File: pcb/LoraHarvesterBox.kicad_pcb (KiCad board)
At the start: 4 copper layers, 48 x 45.5 mm, 44 parts, among them J1 Conn_01x02_Pin, J2 Conn_01x02_Pin, J3 Conn_01x02_Pin, J4 Conn_01x04_Socket, J5 Conn_01x04_Socket, J6 Conn_01x04_Socket, J7 Conn_01x04_Socket, J8 Conn_01x06_Socket, SW1 SSSS811101, SW2 TS-1088-AR02016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

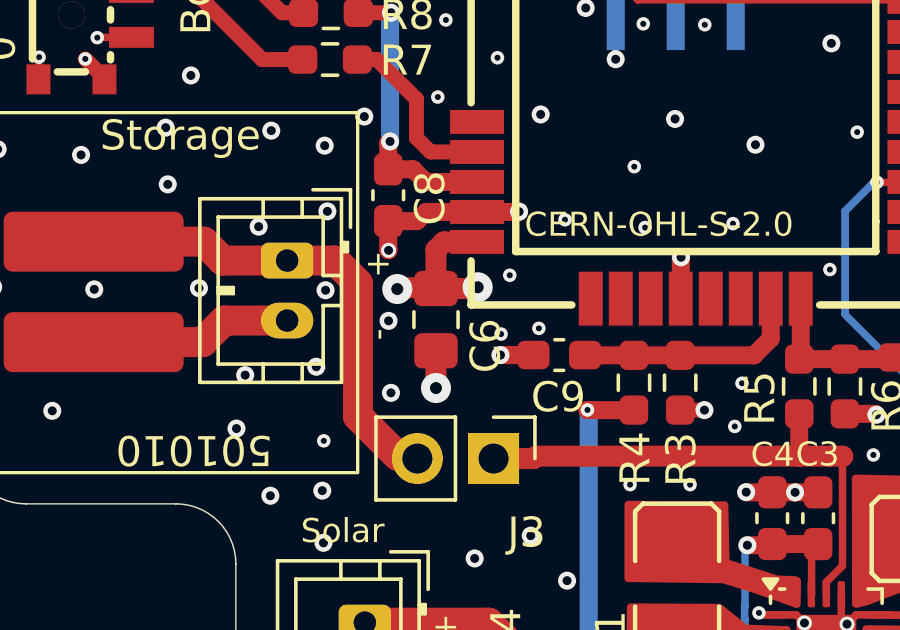
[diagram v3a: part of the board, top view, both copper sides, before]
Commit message: pcb, sch, doc: remove C as RAK31762 has 10uF+100nF already internally
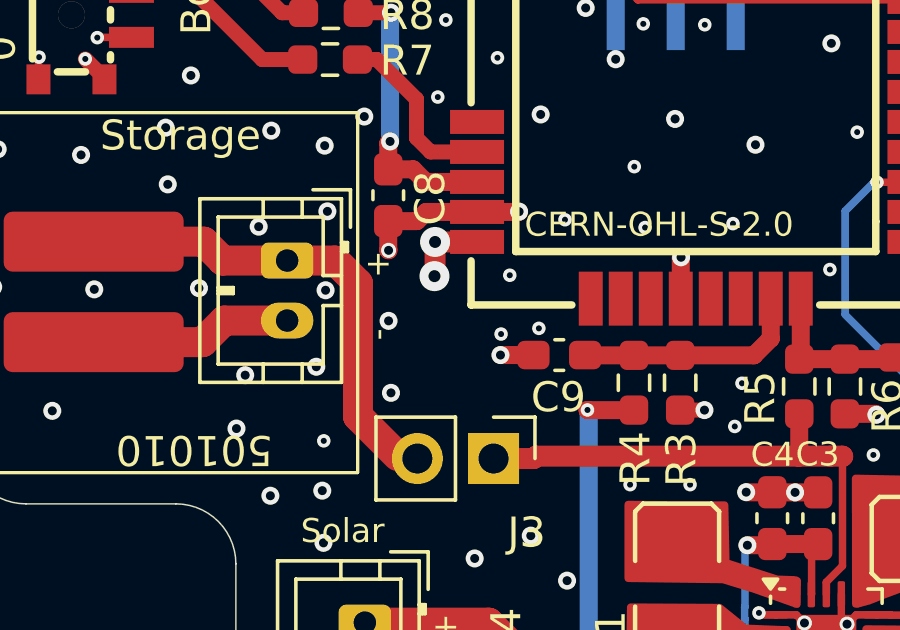
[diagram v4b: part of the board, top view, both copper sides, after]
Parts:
- removed C6: C, Capacitor_SMD:C_0805_2012Metric_Pad1.18x1.45mm_HandSolder
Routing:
- net +3V0: track 16.0 -> 13.1 mm
- net GND: track 59.4 -> 58.1 mm, vias 186 -> 185
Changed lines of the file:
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@@
 		)
 	)
-	(footprint "Capacitor_SMD:C_0805_2012Metric_Pad1.18x1.45mm_HandSolder"
-		(layer "F.Cu")
-		(at 116.67 82.86 90)
-		(descr "Capacitor SMD 0805 (2012 Metric), square (rectangular) end terminal, IPC-7351 nominal with elongated pad for handsoldering. (Body size source: IPC-SM-782 page 76, https://www.pcb-3d.com/wordpress/wp-content/uploads/ipc-sm-782a_amendment_1_and_2.pdf, https://docs.google.com/spreadsheets/d/1BsfQQcO9C6DZCsRaXUlFlo91Tg2WpOkGARC1WS5S8t0/edit?usp=sharing), generated with kicad-footprint-generator")
-		(tags "capacitor handsolder")
-		(property "Reference" "C6"
-			(at -0.87 1.66 90)
-			(layer "F.SilkS")
-			(effects
-				(font
-					(size 1 1)
-					(thickness 0.15)
-				)
-			)
-		)
-		(property "Value" "C"
-			(at 0 1.68 90)
-			(layer "F.Fab")
-			(hide yes)
-			(effects
-				(font
-					(size 1 1)
-					(thickness 0.15)
-				)
-			)
-		)
-		(property "Datasheet" "~"
-			(at 0 0 90)
-			(layer "F.Fab")
-			(hide yes)
-			(effects
-				(font
-					(size 1.27 1.27)
-					(thickness 0.15)
-				)
-			)
-		)
-		(property "Description" "Unpolarized capacitor"
-			(at 0 0 90)
-			(layer "F.Fab")
-			(hide yes)
-			(effects
-				(font
-					(size 1.27 1.27)
-					(thickness 0.15)
-				)
-			)
-		)
-		(property ki_fp_filters "C_*")
-		(sheetname "/")
-		(sheetfile "LoraHarvesterBox.kicad_sch")
-		(attr smd)
-		(fp_line
-			(start -0.261252 -0.735)
-			(end 0.261252 -0.735)
-			(stroke
-				(width 0.12)
-				(type solid)
-			)
-			(layer "F.SilkS")
-		)
-		(fp_line
-			(start -0.261252 0.735)
-			(end 0.261252 0.735)
-			(stroke
-				(width 0.12)
-				(type solid)
-			)
-			(layer "F.SilkS")
-		)
-		(fp_line
-			(start 1.88 -0.98)
-			(end 1.88 0.98)
-			(stroke
-				(width 0.05)
-				(type solid)
-			)
-			(layer "F.CrtYd")
-		)
-		(fp_line
-			(start -1.88 -0.98)
-			(end 1.88 -0.98)
-			(stroke
-				(width 0.05)
-				(type solid)
-			)
-			(layer "F.CrtYd")
-		)
-		(fp_line
-			(start 1.88 0.98)
-			(end -1.88 0.98)
-			(stroke
-				(width 0.05)
-				(type solid)
-			)
-			(layer "F.CrtYd")
-		)
-		(fp_line
-			(start -1.88 0.98)
-			(end -1.88 -0.98)
-			(stroke
-				(width 0.05)
-				(type solid)
-			)
-			(layer "F.CrtYd")
-		)
-		(fp_line
-			(start 1 -0.625)
-			(end 1 0.625)
-			(stroke
-				(width 0.1)
-				(type solid)
-			)
-			(layer "F.Fab")
-		)
-		(fp_line
-			(start -1 -0.625)
-			(end 1 -0.625)
-			(stroke
-				(width 0.1)
-				(type solid)
-			)
-			(layer "F.Fab")
-		)
-		(fp_line
-			(start 1 0.625)
-			(end -1 0.625)
-			(stroke
-				(width 0.1)
-				(type solid)
-			)
-			(layer "F.Fab")
-		)
-		(fp_line
-			(start -1 0.625)
-			(end -1 -0.625)
-			(stroke
-				(width 0.1)
-				(type solid)
-			)
-			(layer "F.Fab")
-		)
-		(fp_text user "${REFERENCE}"
-			(at 0 0 90)
-			(layer "F.Fab")
-			(effects
-				(font
-					(size 0.5 0.5)
-					(thickness 0.08)
-				)
-			)
-		)
-		(pad "1" smd roundrect
-			(at -1.0375 0 90)
-			(size 1.175 1.45)
-			(layers "F.Cu" "F.Mask" "F.Paste")
-			(roundrect_rratio 0.212766)
-			(net 2 "GND")
-			(pintype "passive")
-		)
-		(pad "2" smd roundrect
-			(at 1.0375 0 90)
-			(size 1.175 1.45)
-			(layers "F.Cu" "F.Mask" "F.Paste")
-			(roundrect_rratio 0.212766)
-			(net 3 "+3V0")
-			(pintype "passive")
-		)
-		(embedded_fonts no)
-		(model "${KICAD9_3DMODEL_DIR}/Capacitor_SMD.3dshapes/C_0805_2012Metric.step"
-			(offset
-				(xyz 0 0 0)
-			)
-			(scale
-				(xyz 1 1 1)
-			)
-			(rotate
-				(xyz 0 0 0)
-			)
-		)
-	)
 	(footprint "Resistor_SMD:R_0603_1608Metric_Pad0.98x0.95mm_HandSolder"
 		(layer "F.Cu")
@@
 	)
 	(segment
-		(start 116.67 83.8975)
-		(end 116.67 85.14)
-		(width 0.7)
-		(layer "F.Cu")
-		(net 2)
-	)
-	(segment
 		(start 132.27 92.71)
 		(end 131.83 92.71)
@@
 	)
 	(via
-		(at 116.67 85.14)
-		(size 1)
-		(drill 0.4)
-		(layers "F.Cu" "B.Cu")
-		(net 2)
-	)
-	(via
 		(at 123.85 57.8)
 		(size 0.6)
@@
 	)
 	(segment
-		(start 116.67 81.8225)
-		(end 116.67 80.53)
+		(start 116.64 81.39)
+		(end 116.64 80.27)
 		(width 0.7)
 		(layer "F.Cu")
@@
 	)
 	(segment
-		(start 118.06 81.78)
-		(end 118.0175 81.8225)
-		(width 0.7)
-		(layer "F.Cu")
-		(net 3)
-	)
-	(segment
-		(start 116.93 80.27)
-		(end 118.04 80.27)
+		(start 118.04 80.27)
+		(end 116.64 80.27)
 		(width 0.7)
 		(layer "F.Cu")
@@
 	)
 	(segment
-		(start 116.77 81.7975)
-		(end 115.4225 81.7975)
+		(start 116.62 81.41)
+		(end 116.64 81.39)
 		(width 0.7)
 		(layer "F.Cu")
@@
 	)
 	(segment
-		(start 116.67 80.53)
-		(end 116.93 80.27)
-		(width 0.7)
-		(layer "F.Cu")
-		(net 3)
-	)
-	(segment
 		(start 106.52 68.95)
 		(end 105.37 68.95)
@@
 	)
 	(segment
-		(start 118.0175 81.8225)
-		(end 116.67 81.8225)
-		(width 0.7)
-		(layer "F.Cu")
-		(net 3)
-	)
-	(segment
 		(start 137.78 87.18)
 		(end 137.79 87.17)
@@
 	)
 	(via
+		(at 116.62 81.41)
+		(size 1)
+		(drill 0.4)
+		(layers "F.Cu" "B.Cu")
+		(net 3)
+	)
+	(via
 		(at 114.32 66.44)
 		(size 0.6)
@@
 	)
 	(via
-		(at 118.06 81.78)
+		(at 116.64 80.27)
 		(size 1)
 		(drill 0.4)
@@
 		(layers "F.Cu" "B.Cu")
 		(net 3)
-	)
-	(via
-		(at 115.38 81.84)
-		(size 1)
-		(drill 0.4)
-		(layers "F.Cu" "B.Cu")
-		(net 3)

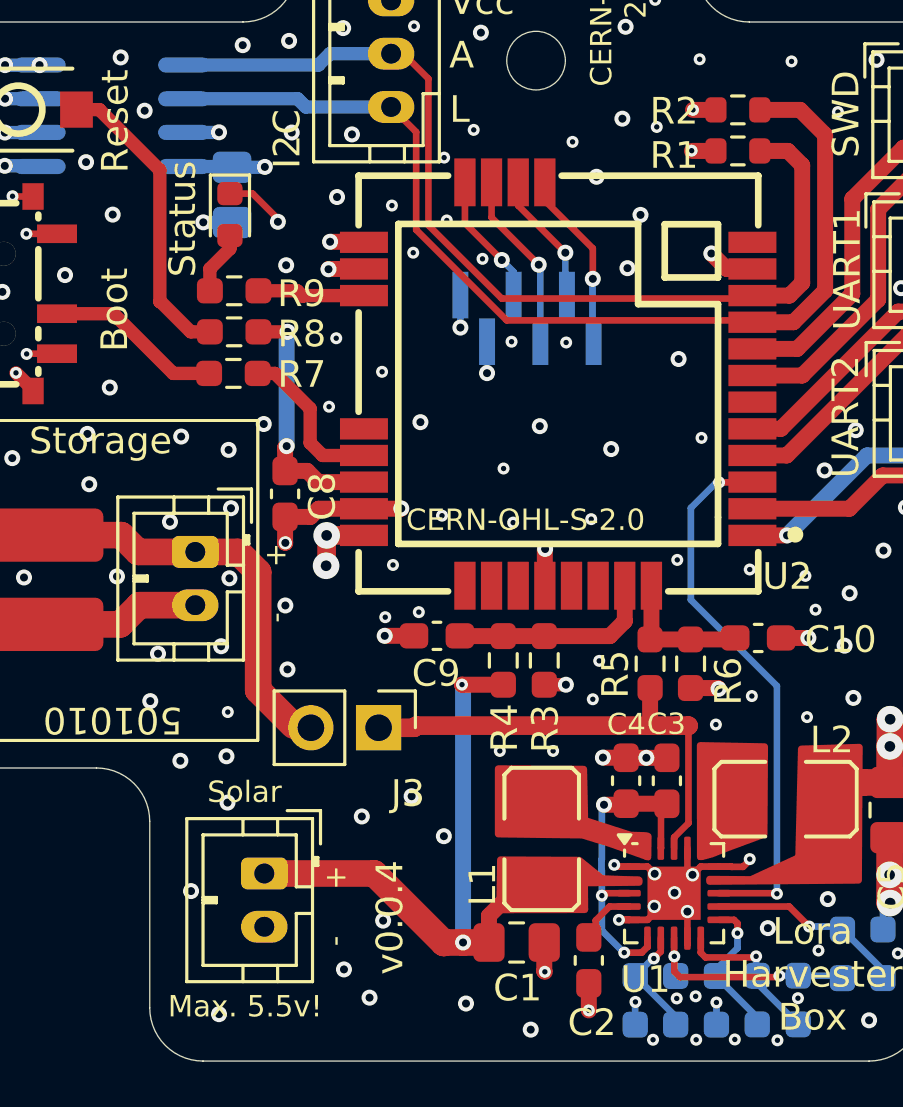
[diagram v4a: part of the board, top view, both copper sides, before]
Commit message: pcb, sch, doc: make more pins available on the back
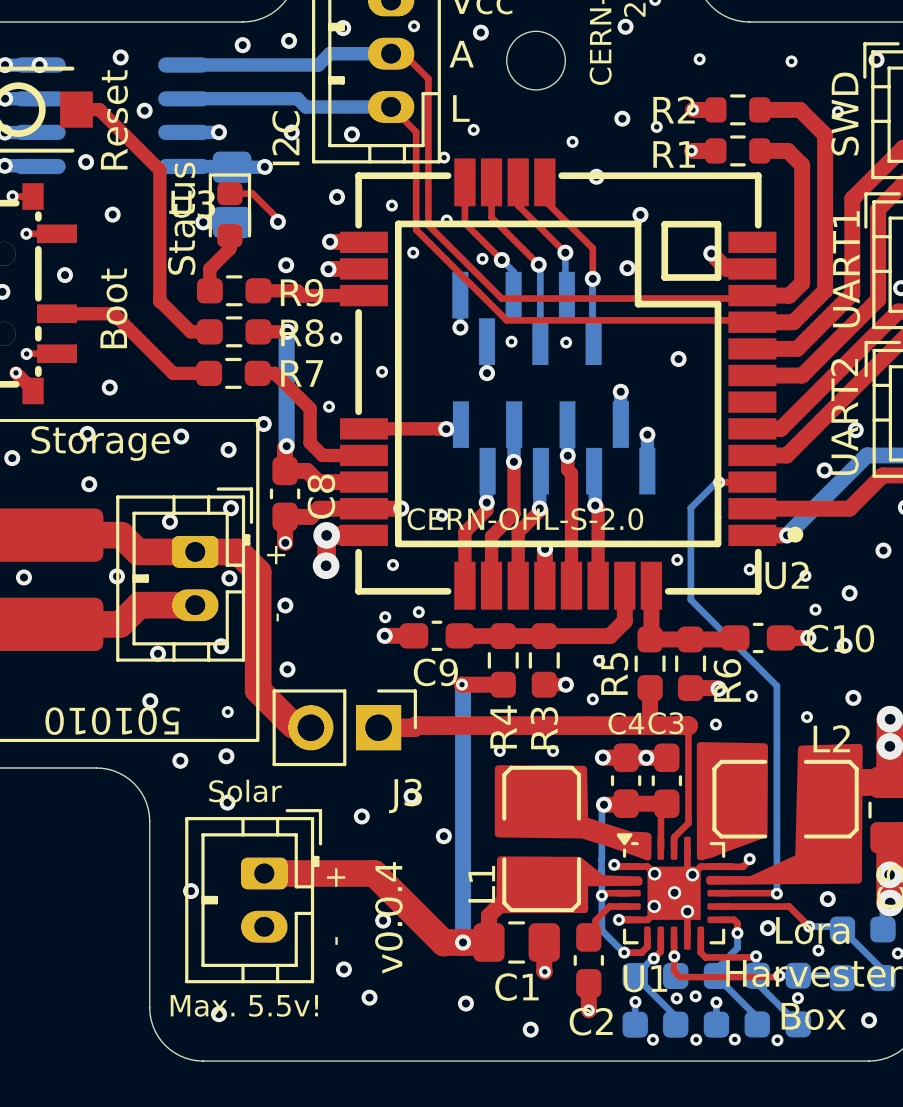
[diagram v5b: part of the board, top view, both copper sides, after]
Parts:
- added J9: Conn_01x08_Socket, Connector_PinHeader_1.00mm:PinHeader_1x08_P1.00mm_Vertical_SMD_Pin1Left, B.Cu at (125.2, 77.0)
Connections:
- U2 pad 20: unconnected-(U2-PA9-Pad20) -> Net-(J9-Pin_1)
- U2 pad 25: unconnected-(U2-PA10/PIN_A3-Pad25) -> Net-(J9-Pin_2)
- U2 pad 26: unconnected-(U2-PB2/PIN_A2-Pad26) -> Net-(J9-Pin_3)
- U2 pad 27: unconnected-(U2-PB12-Pad27) -> Net-(J9-Pin_4)
- U2 pad 29: unconnected-(U2-PA0-Pad29) -> Net-(J9-Pin_5)
- U2 pad 30: unconnected-(U2-PB5-Pad30) -> Net-(J9-Pin_6)
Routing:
- net Net-(J9-Pin_3): track 0.00 -> 6.39 mm, vias 0 -> 1
- net Net-(J9-Pin_5): track 0.00 -> 6.10 mm, vias 0 -> 1
- net Net-(J9-Pin_2): track 0.00 -> 4.61 mm, vias 0 -> 1
- net Net-(J9-Pin_4): track 0.00 -> 4.60 mm, vias 0 -> 1
- net Net-(J9-Pin_6): track 0.00 -> 4.31 mm, vias 0 -> 1
- net Net-(J9-Pin_1): track 0.00 -> 3.71 mm, vias 0 -> 1
- net +3V0: track 13.1 -> 14.3 mm, vias 9 -> 10
- net /VSOLAR: track 26.5 -> 25.7 mm
- net GND: track 58.1 -> 58.5 mm, vias 185 -> 179
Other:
- board text added: "."
- board text added: "FRAM"
- board text added: "GPIO"
- board text added: "PA10-PA3"
- board text added: "PA9"
- board text added: "PB12"
- board text added: "PB2-PA2"
- board text added: "PB5"
- board text removed: "CERN Open Hardware Licence Version 2 Strongly Reciprocal"

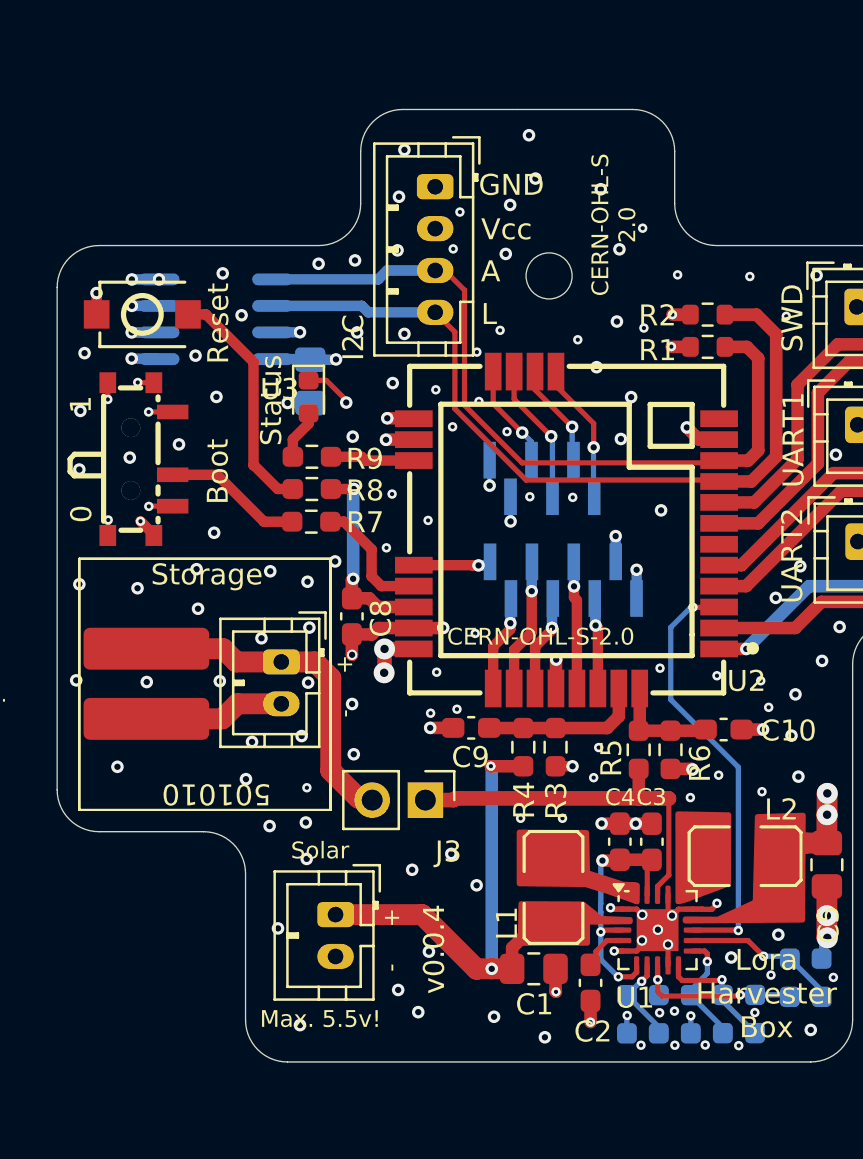
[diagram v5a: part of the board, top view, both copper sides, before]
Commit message: sch, pcb, doc: remove FRAM to the top layer
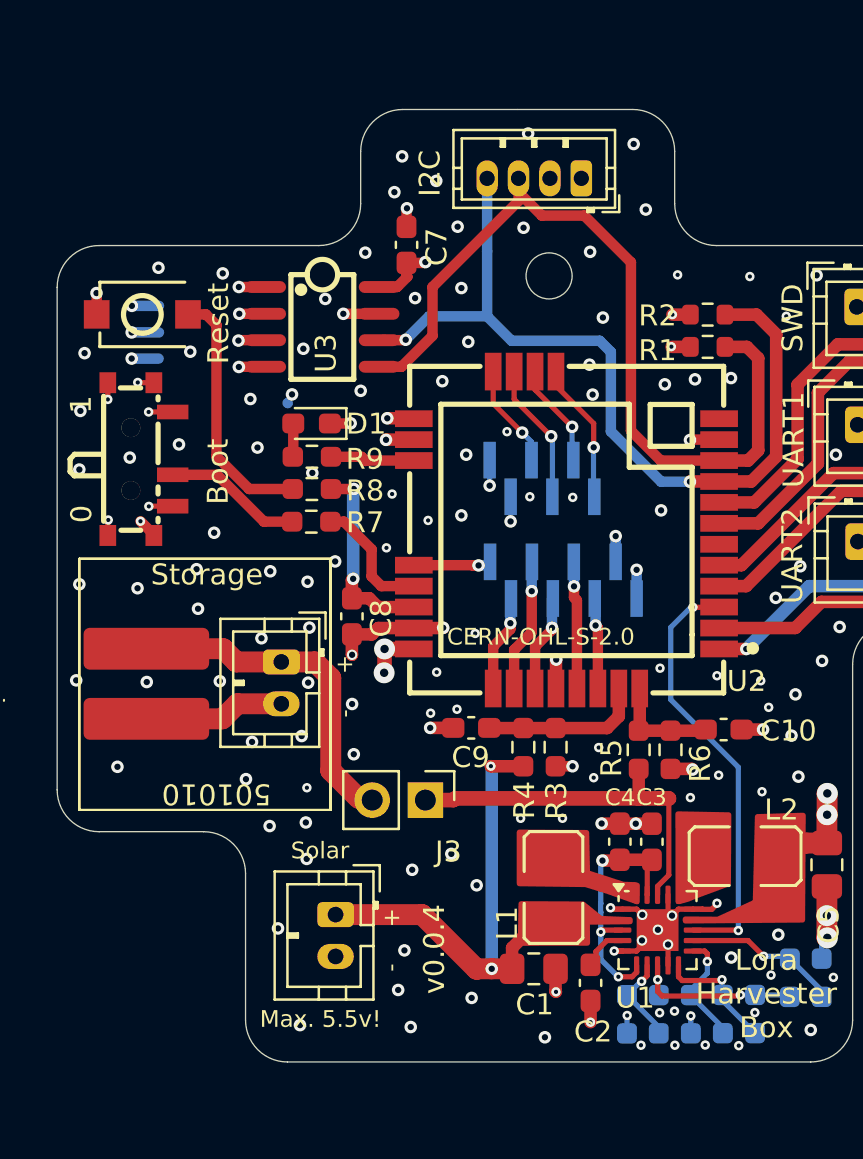
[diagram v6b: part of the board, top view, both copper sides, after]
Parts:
- C7: footprint Capacitor_SMD:C_0805_2012Metric_Pad1.18x1.45mm_HandSolder -> Capacitor_SMD:C_0603_1608Metric_Pad1.08x0.95mm_HandSolder; moved to F.Cu
- D1: footprint LED_SMD:LED_0603_1608Metric -> LED_SMD:LED_0603_1608Metric_Pad1.05x0.95mm_HandSolder
- J7: footprint Connector_JST:JST_PH_B4B-PH-K_1x04_P2.00mm_Vertical -> Connector_JST:JST_ZH_B4B-ZR_1x04_P1.50mm_Vertical
- U3: moved to F.Cu
- moved C7 7.98 mm to (117.7, 61.0), turned to -90 degrees
- moved J7 6.99 mm to (126.0, 57.8), turned to 180 degrees
- moved U3 5.10 mm to (113.7, 64.9), turned to -90 degrees
- moved D1 1.28 mm to (113.2, 69.5), turned to 180 degrees
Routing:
- net /SDA: track 36.3 -> 41.5 mm
- net /SCL: track 38.8 -> 41.4 mm, vias 0 -> 2
- net GND: track 58.5 -> 60.5 mm, vias 179 -> 180
- net Net-(R8-Pad1): track 11.4 -> 12.1 mm
- net Net-(D1-A): track 2.38 -> 1.65 mm
- net +3V0: track 14.3 -> 14.8 mm
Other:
- board text removed: "A"
- board text removed: "CERN-OHL-S 2.0"
- board text removed: "FRAM"
- board text removed: "L"
- board text removed: "Status"
